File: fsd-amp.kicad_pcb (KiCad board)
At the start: 2 copper layers, 100 x 60 mm, 20 parts, among them J1001 Screw_Terminal_01x06, J1004 AudioJack2_Ground_Switch, Q1001 FZT 653 ZET, Q1002 FZT 653 ZET, Q1003 FZT 753 ZET, Q1004 Q_NPN_BCE, Q1005 Q_PNP_BCE, Q1006 Q_NPN_BCE

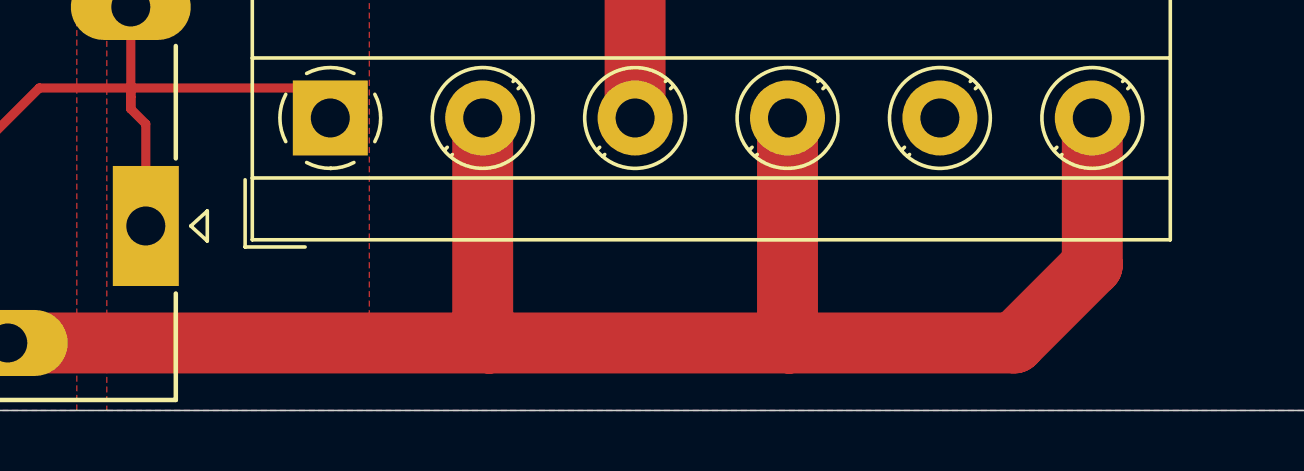
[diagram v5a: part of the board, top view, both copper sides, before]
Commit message: add connection labels on silkT
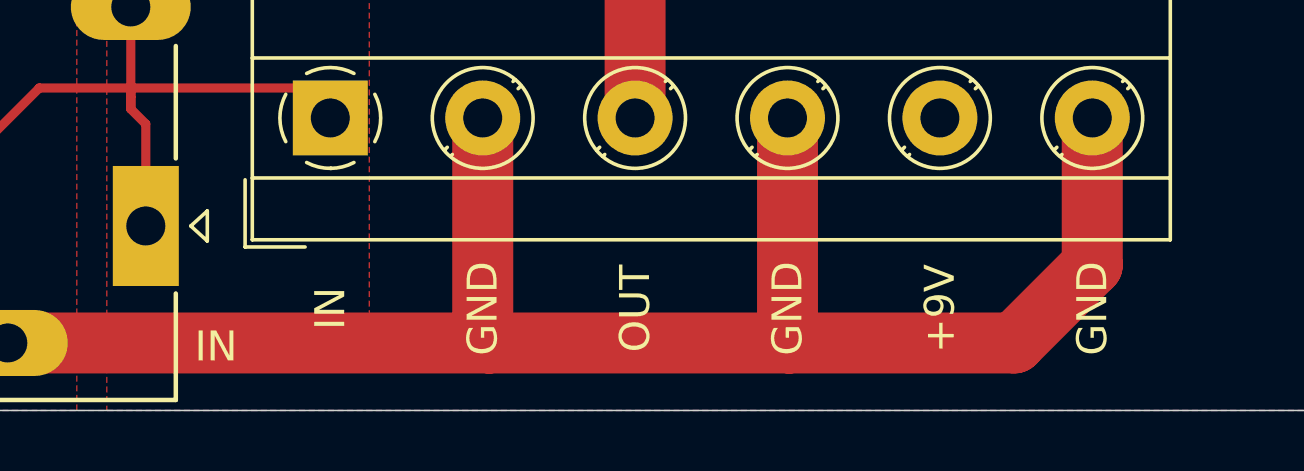
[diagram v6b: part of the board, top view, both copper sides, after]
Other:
- board text added: "+9V"
- board text added: "GND"
- board text added: "IN"
- board text added: "OUT"
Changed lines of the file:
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@@
 		(pad_to_mask_clearance 0)
 		(allow_soldermask_bridges_in_footprints no)
-		(grid_origin 100 110)
+		(grid_origin 157.95 100.25)
 		(pcbplotparams
 			(layerselection 0x00010fc_ffffffff)
@@
 		(layer "Edge.Cuts")
 	)
+	(gr_text "+9V"
+		(at 178.27 106.6 90)
+		(layer "F.SilkS" knockout)
+		(effects
+			(font
+				(size 1 1)
+				(thickness 0.15)
+			)
+		)
+	)
+	(gr_text "GND"
+		(at 163.03 106.6 90)
+		(layer "F.SilkS" knockout)
+		(effects
+			(font
+				(size 1 1)
+				(thickness 0.15)
+			)
+		)
+	)
+	(gr_text "GND"
+		(at 173.19 106.6 90)
+		(layer "F.SilkS" knockout)
+		(effects
+			(font
+				(size 1 1)
+				(thickness 0.15)
+			)
+		)
+	)
+	(gr_text "OUT"
+		(at 168.11 106.6 90)
+		(layer "F.SilkS" knockout)
+		(effects
+			(font
+				(size 1 1)
+				(thickness 0.15)
+			)
+		)
+	)
+	(gr_text "IN"
+		(at 157.95 106.6 90)
+		(layer "F.SilkS" knockout)
+		(effects
+			(font
+				(size 1 1)
+				(thickness 0.15)
+			)
+		)
+	)
+	(gr_text "GND"
+		(at 183.35 106.6 90)
+		(layer "F.SilkS" knockout)
+		(effects
+			(font
+				(size 1 1)
+				(thickness 0.15)
+			)
+		)
+	)
+	(gr_text "IN"
+		(at 154.14 107.87 0)
+		(layer "F.SilkS" knockout)
+		(effects
+			(font
+				(size 1 1)
+				(thickness 0.15)
+			)
+		)
+	)
 	(via

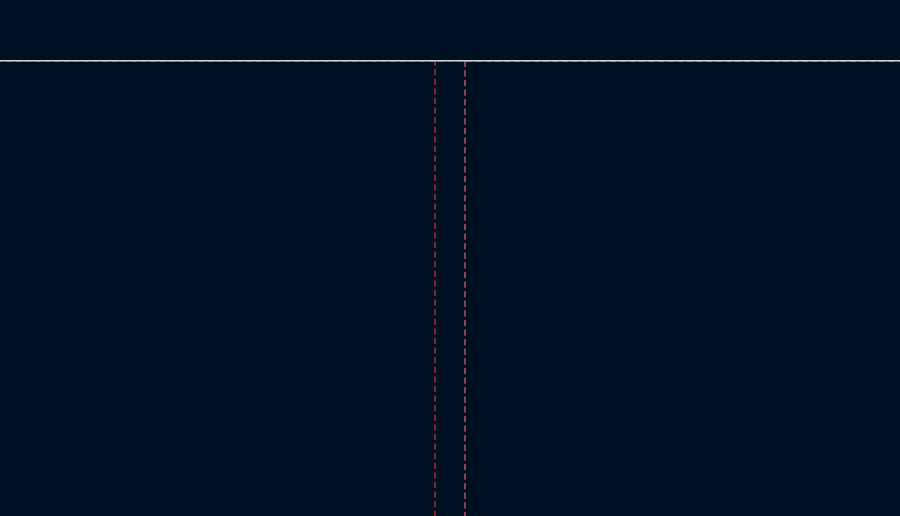
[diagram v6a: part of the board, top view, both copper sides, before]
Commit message: add title at f.silk
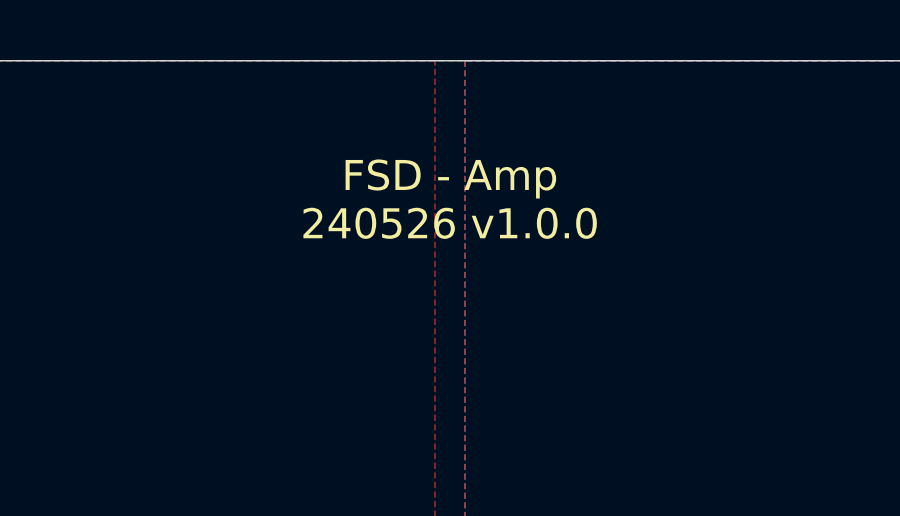
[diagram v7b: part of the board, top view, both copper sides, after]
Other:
- board text added: "FSD - Amp 240526 v1.0.0"
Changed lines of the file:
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@@
+		)
+	)
+	(gr_text "FSD - Amp\n240526 v1.0.0"
+		(at 150 53.26 0)
+		(layer "F.SilkS" knockout)
+		(effects
+			(font
+				(size 1 1)
+				(thickness 0.15)
+			)
+			(justify top)
 		)
 	)

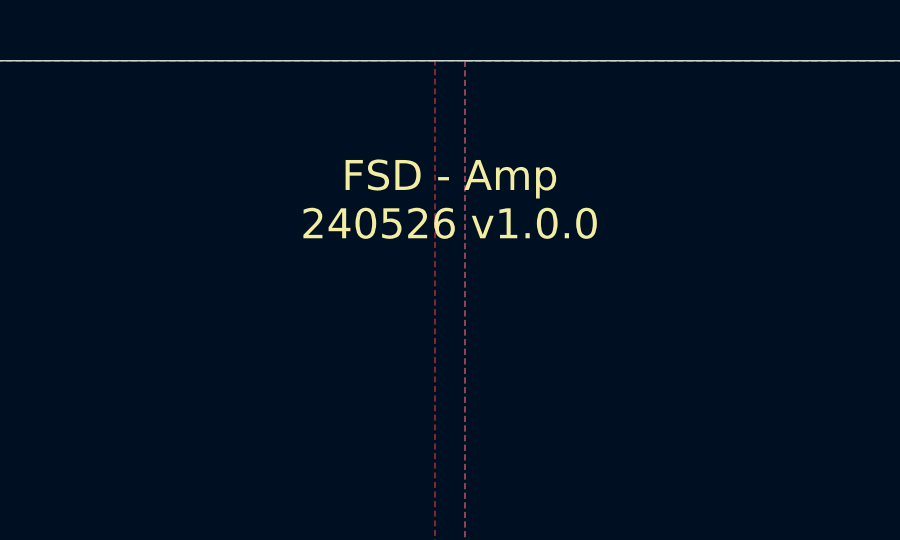
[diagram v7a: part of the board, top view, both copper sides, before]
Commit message: add variable substitution for date and revision
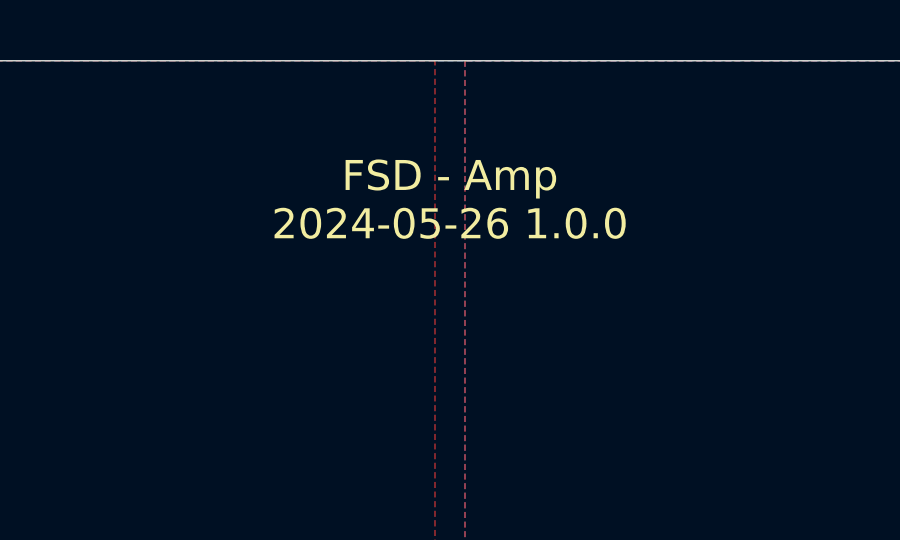
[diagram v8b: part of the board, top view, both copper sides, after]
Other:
- board text added: "FSD - Amp ${ISSUE_DATE} ${REVISION}"
- board text removed: "FSD - Amp 240526 v1.0.0"
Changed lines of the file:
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@@
 	(title_block
 		(title "FSD-Amp")
-		(date "2024-05-24")
+		(date "2024-05-26")
 		(rev "1.0.0")
 	)
@@
 		)
 	)
-	(gr_text "FSD - Amp\n240526 v1.0.0"
+	(gr_text "FSD - Amp\n${ISSUE_DATE} ${REVISION}"
 		(at 150 53.26 0)
 		(layer "F.SilkS" knockout)
